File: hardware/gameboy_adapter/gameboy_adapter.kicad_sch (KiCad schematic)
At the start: 3 parts, among them J1 CART SLOT TOP ROW, J2 GBA_Slot, SW1 SW_SPDT

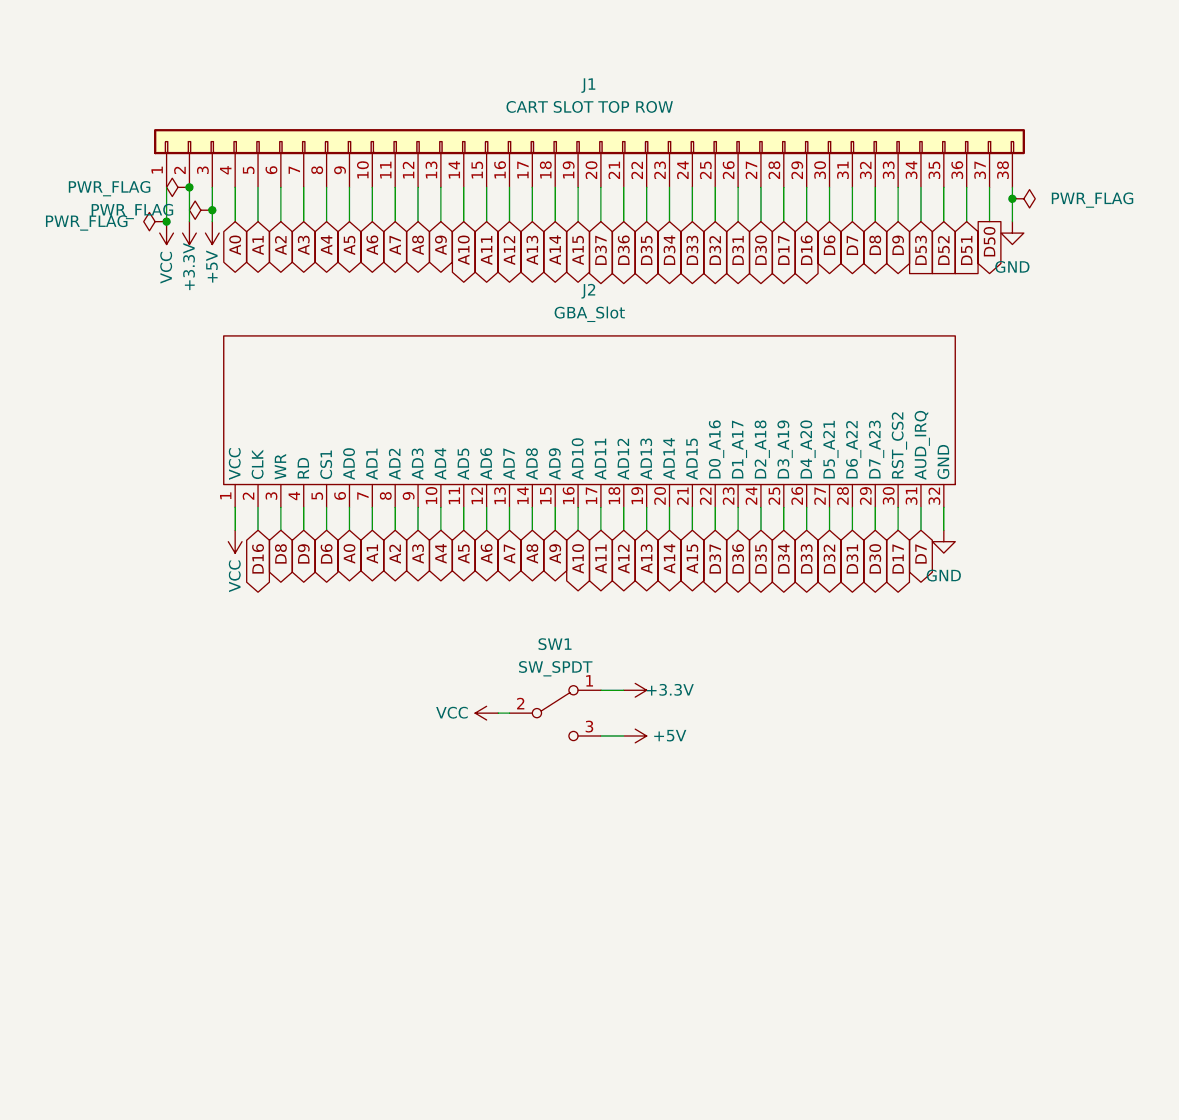
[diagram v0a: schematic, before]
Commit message: update schematic
propagate changes from main PCB to GB breakout
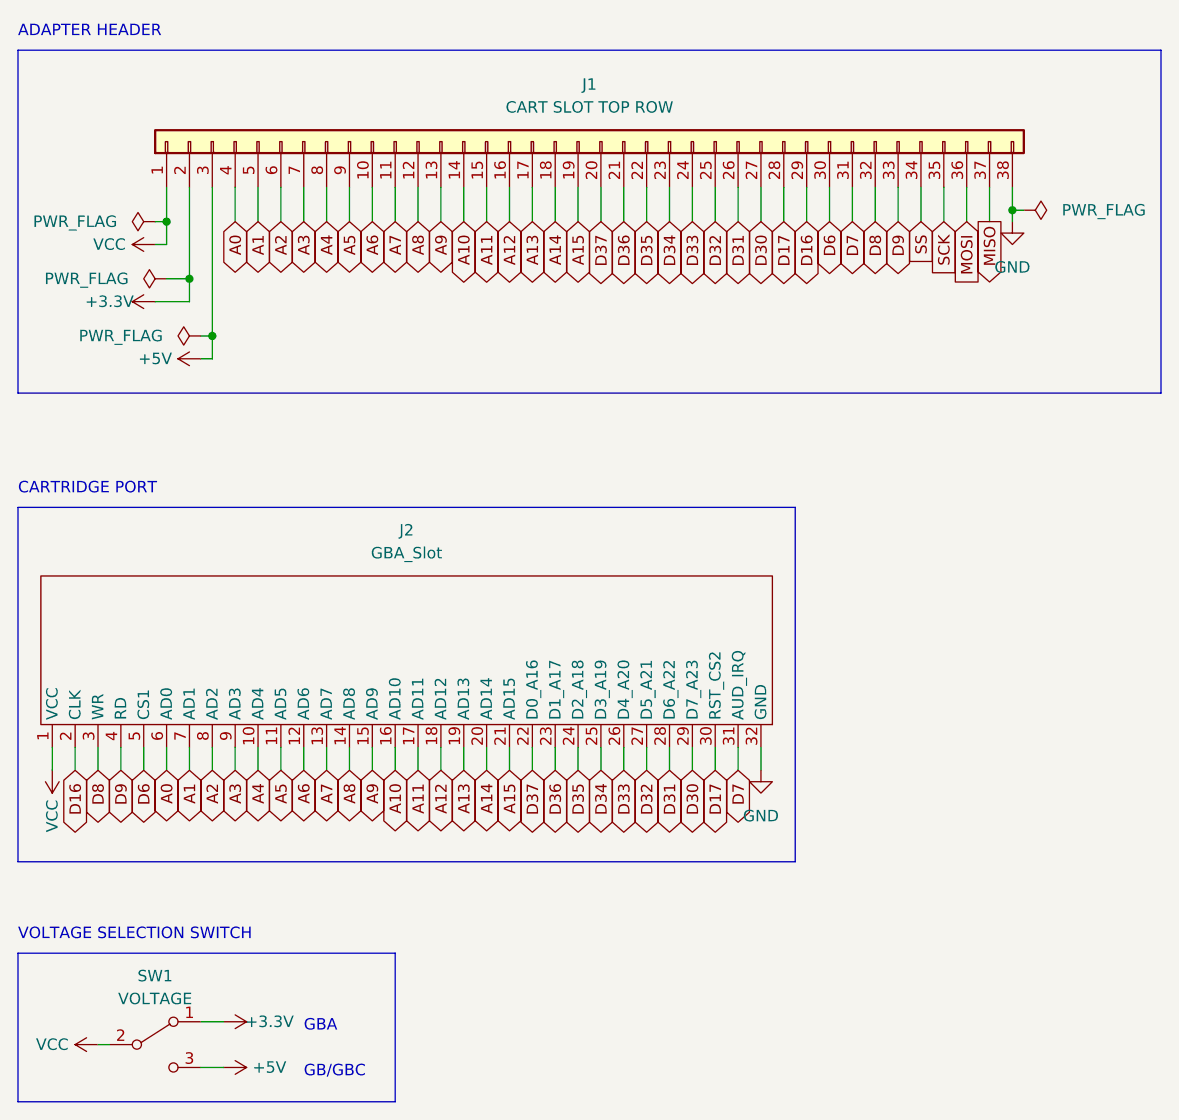
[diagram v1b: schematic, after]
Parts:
- J2: footprint (none) -> !OSCR:GBA_Slot; symbol sanni:GBA_Slot -> !OSCR:GBA_Slot
- SW1: value SW_SPDT -> VOLTAGE; footprint (none) -> Button_Switch_THT:SW_CuK_OS102011MA1QN1_SPDT_Angled
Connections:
- net +3V3 renamed +3.3V
- net D50 renamed MISO
- net D51 renamed MOSI
- net D52 renamed SCK
- net D53 renamed SS
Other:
- note added: "ADAPTER HEADER"
- note added: "CARTRIDGE PORT"
- note added: "GB/GBC"
- note added: "GBA"
- note added: "VOLTAGE SELECTION SWITCH"
- title: OSCR GAMEBOY ADAPTER -> OSCR SHIELD - GB/GBC/GBA BREAKOUT
- moved on the sheet: J2, SW1
